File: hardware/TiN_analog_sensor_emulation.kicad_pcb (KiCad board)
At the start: 2 copper layers, 100 x 100 mm, 179 parts, among them J1 Conn_02x02_Odd_Even, J10 Conn_01x01_Male, J2 Conn_01x04_Male, J3 Micro_SD_Card, J4 BOOT0, J5 Conn_01x03_Male, J6 display, J7 Barrel_Jack, J8 Conn_02x08_Odd_Even, J9 Conn_01x01_Male, SW2 SW_right, SW3 SW_middle2, SW4 SW_top, SW5 SW_middle, SW6 SW_bot, SW7 SW_Left, U1 STM32F042C6Tx, U10 MCP42010, U11 ADA4898-3, U12 ADA4898-3, U13 MCP42010, U14 MCP42010, U15 MCP42050, U16 MCP42050, U17 MCP42050, U18 LT1529CQ#PBF, U19 LT1528CQ, U2 ADA4898-3, U3 ADA4898-3, U4 MCP42010, U5 ADA4898-3, U6 ADA4898-3, U7 MCP42010, U8 ADA4898-3, U9 ADA4898-3, Y1 Crystal_GND24

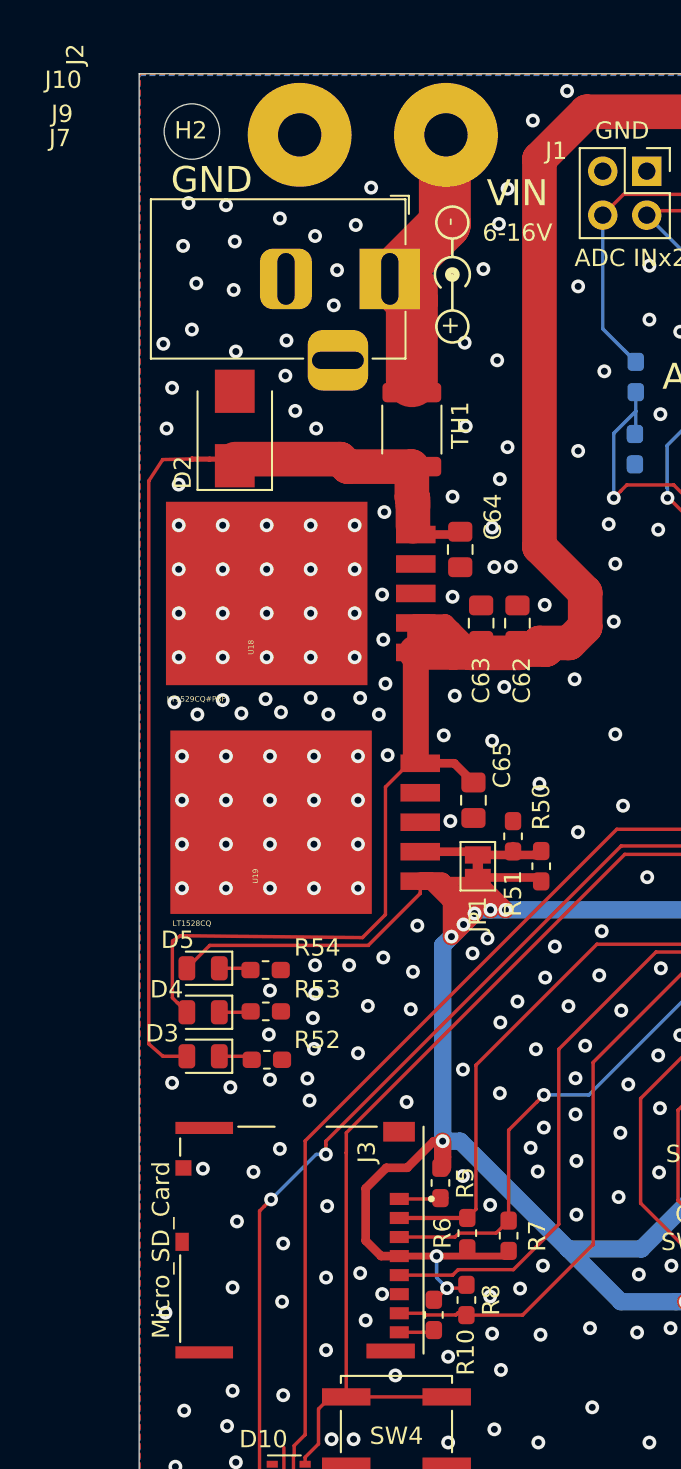
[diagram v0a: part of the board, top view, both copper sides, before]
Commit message: dodano gerbery i obrócono kartę uSD (teraz na bottom)
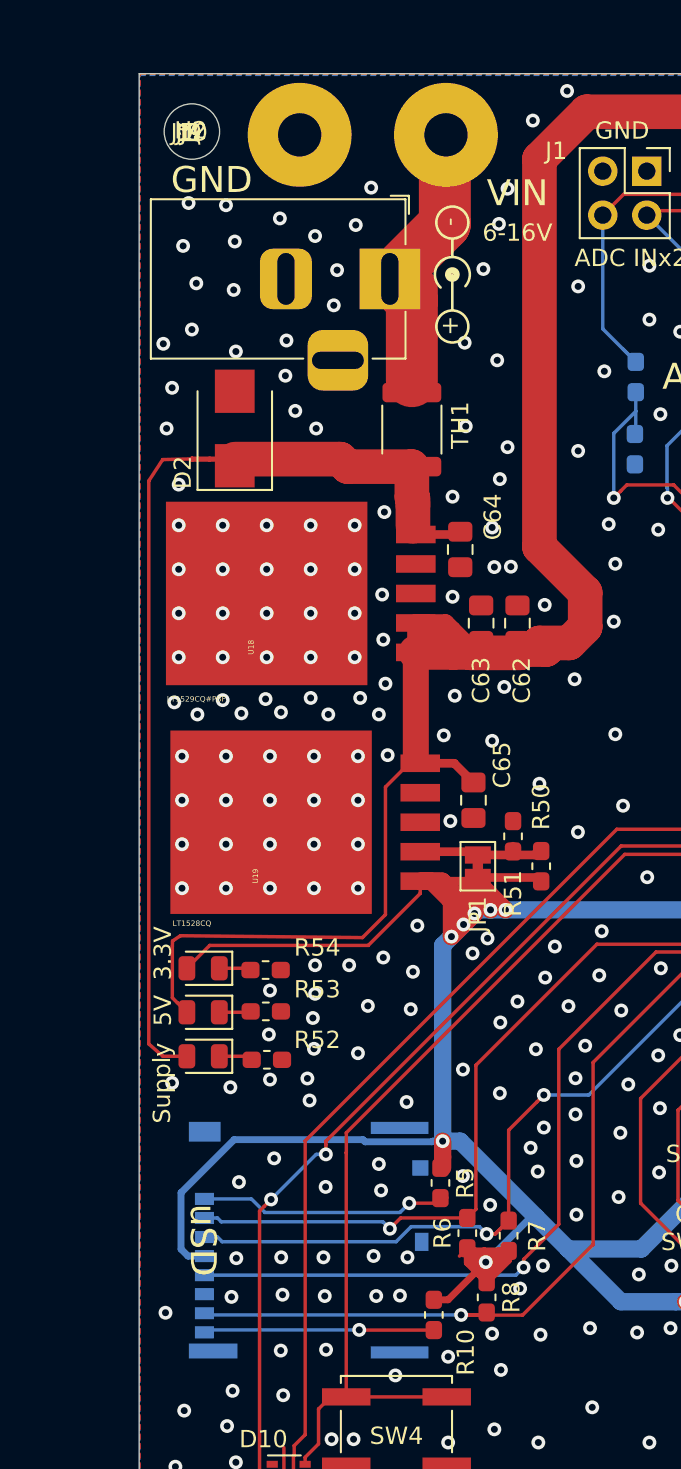
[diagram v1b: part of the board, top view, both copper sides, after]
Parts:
- J3: moved to B.Cu
- moved R8 1.18 mm to (115.1, 120.7)
- renumbered D5 to 3.3V, D4 to 5V, D3 to Supply
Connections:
- J3 pad 10: (no net) -> GND
- J3 pad P1: (no net) -> GND
- J3 pad P2: (no net) -> GND
- J3 pad P3: (no net) -> GND
- J3 pad P4: (no net) -> GND
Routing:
- net +3.3VA: track 337.2 -> 360.1 mm, vias 20 -> 19
- net /MCU/SDMOSI: track 33.3 -> 46.1 mm, vias 2 -> 3
- net /MCU/SDMISO: track 38.4 -> 51.0 mm, vias 0 -> 1
- net /MCU/SD~SS: track 34.9 -> 46.6 mm, vias 0 -> 1
- net Net-(J3-Pad1): track 2.78 -> 14.4 mm, vias 0 -> 1
- net /MCU/SDCLK: track 37.0 -> 48.5 mm, vias 0 -> 1
- net Net-(J3-Pad8): track 2.05 -> 13.5 mm, vias 0 -> 1
- net GND: vias 687 -> 690
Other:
- board text added: "uSD"

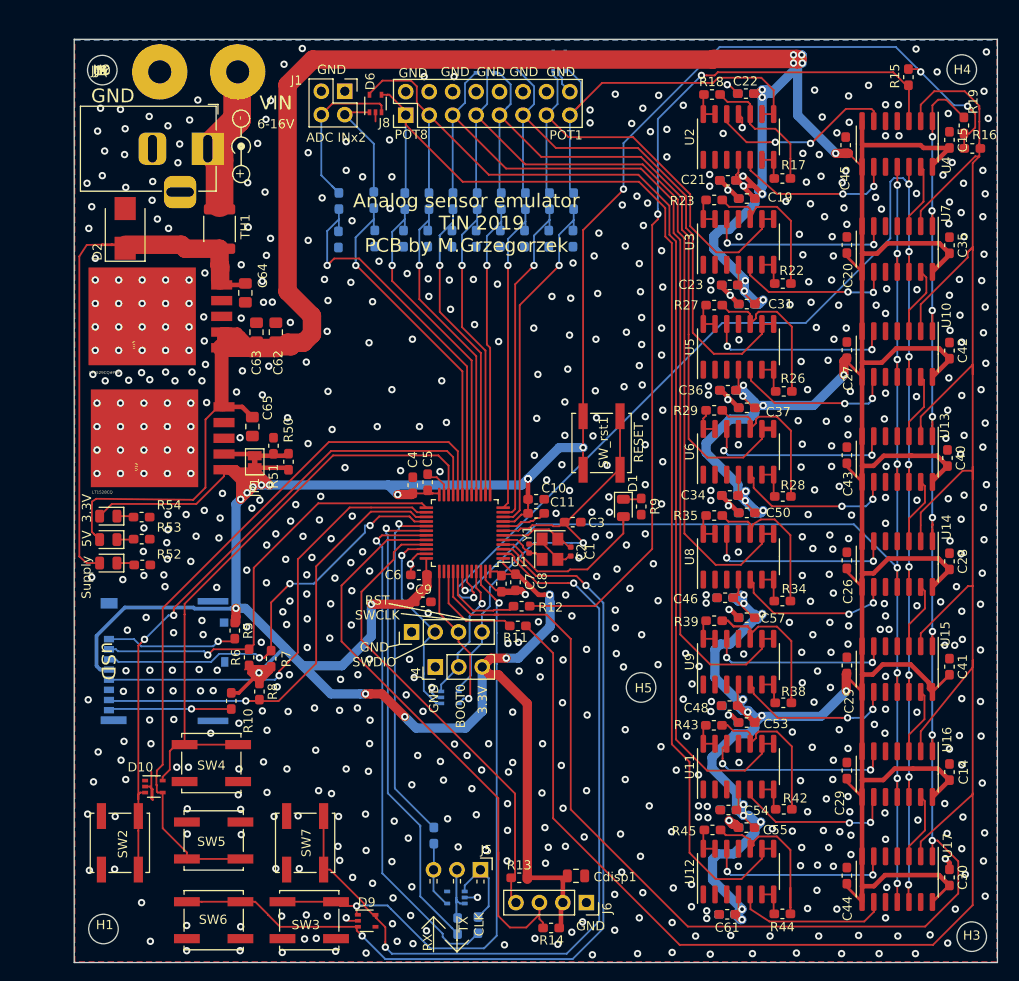
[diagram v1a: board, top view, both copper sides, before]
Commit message: dodano poprawki błędów znalezionych podczas montażu
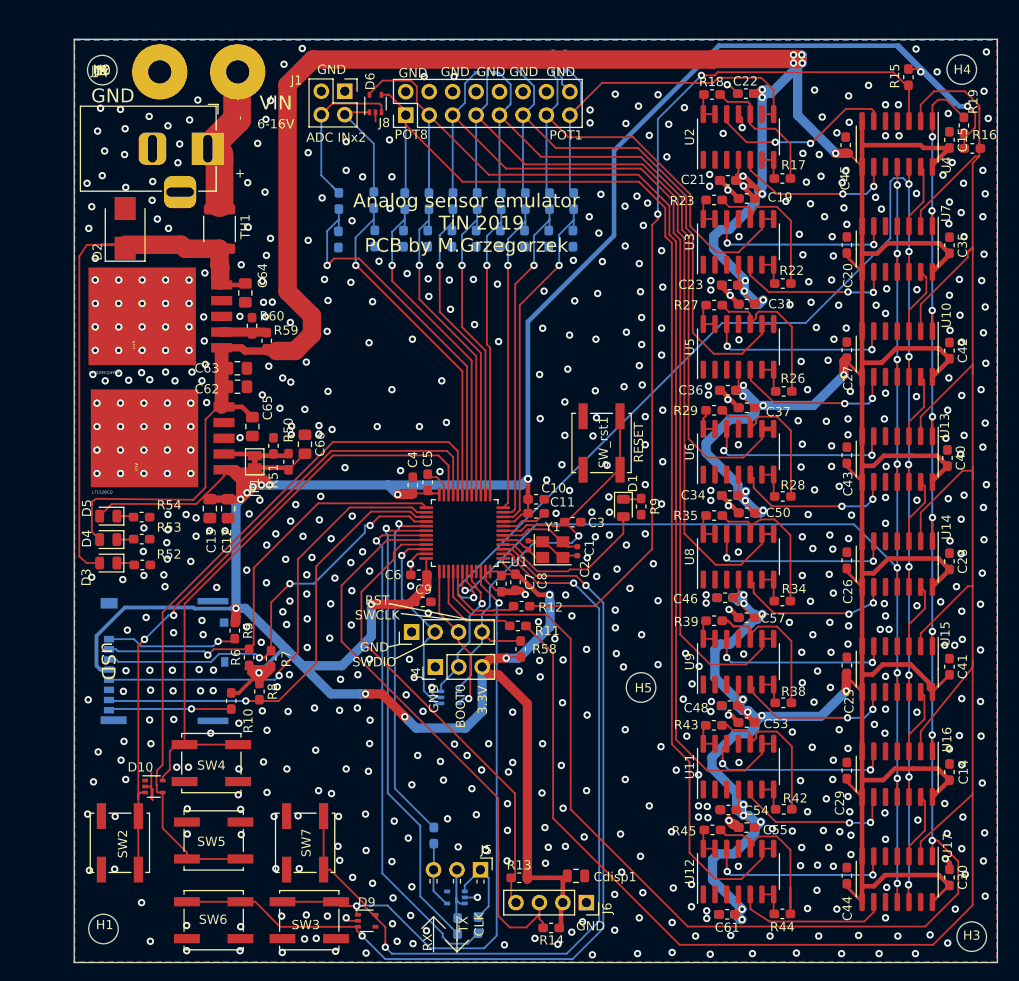
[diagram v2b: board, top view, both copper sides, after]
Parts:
- removed REF**: KiCad-Logo2_5mm_SilkScreen, Symbol:KiCad-Logo2_5mm_SilkScreen
- removed REF**: Symbol_Barrel_Polarity, Symbol:Symbol_Barrel_Polarity
- added C12: 22u, Capacitor_SMD:C_0805_2012Metric_Pad1.15x1.40mm_HandSolder, F.Cu at (111.7, 100.8)
- added C13: 22u, Capacitor_SMD:C_0805_2012Metric_Pad1.15x1.40mm_HandSolder, F.Cu at (109.7, 100.8)
- added C66: 22u, Capacitor_SMD:C_0805_2012Metric_Pad1.15x1.40mm_HandSolder, F.Cu at (120.0, 93.9)
- added R58: 10k', Resistor_SMD:R_0603_1608Metric_Pad1.05x0.95mm_HandSolder, F.Cu at (143.4, 116.0)
- added R59: 110k, Resistor_SMD:R_0603_1608Metric_Pad1.05x0.95mm_HandSolder, F.Cu at (115.9, 82.7)
- added R60: 330k, Resistor_SMD:R_0603_1608Metric_Pad1.05x0.95mm_HandSolder, F.Cu at (114.3, 81.0)
- Y1: footprint Crystal:Crystal_SMD_3225-4Pin_3.2x2.5mm -> symbols:Crystal_SMD_3225-4Pin_3.2x2.5mm
- moved C62 7.22 mm to (112.7, 87.6), turned to 0 degrees
- moved C63 4.42 mm to (112.7, 85.6), turned to 0 degrees
- moved C2 0.72 mm to (149.5, 105.4)
- moved C1 0.35 mm to (144.2, 104.8)
- moved Y1 0.31 mm to (146.8, 105.3), turned to 0 degrees
- renumbered Supply to D3, 5V to D4, 3.3V to D5
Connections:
- J3 pad 10: GND -> (no net)
- J3 pad P1: GND -> (no net)
- J3 pad P2: GND -> (no net)
- J3 pad P3: GND -> (no net)
- J3 pad P4: GND -> (no net)
- SW_rst1 pad 1: +3.3VA -> GND
- U1 pad 44: (no net) -> /MCU/BOOT0
- U1 pad 45: /MCU/BOOT0 -> (no net)
- U18 pad 2: +5V -> Net-(R59-Pad2)
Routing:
- net +3.3VA: track 360.1 -> 393.4 mm, vias 19 -> 17
- net +5V: track 601.1 -> 584.8 mm
- net Net-(R59-Pad2): track 0.00 -> 5.20 mm
- net /MCU/~RST: track 48.5 -> 52.2 mm
- net GND: track 60.2 -> 62.5 mm, vias 690 -> 693
- net Net-(C2-Pad2): track 8.25 -> 9.85 mm
